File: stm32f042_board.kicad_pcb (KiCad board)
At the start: 4 copper layers, 37.8 x 18.8 mm, 24 parts, among them J1 Conn_01x12_Female, J2 Conn_01x12_Female, J3 USB_B_Micro, J5 JTAG/SWD, U1 STM32F042F6Px, U2 MCP1802, U3 USBLC6-2SC6

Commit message: Bug fixes
- Un-migrate to v7 - oshpark not compatibile yet
- Optionally ground USB shield to board via R 0k
- Route Tx/Rx (USB D+/-) as diff pair to breakout pins
- Fix missing +3V3 connection to JTAG pin 1
- Four-layer board
- Remove unnecessary gaps in copper now that board is four layers
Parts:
- added R1: 0k, Resistor_SMD:R_0603_1608Metric, F.Cu at (176.7, 58.6)
- moved G*** 2.10 mm to (175.7, 72.3), turned to -90 degrees
- moved C4 0.55 mm to (161.5, 67.3)
- moved C3 0.19 mm to (164.4, 66.6)
- moved C5 0.19 mm to (164.4, 64.6)
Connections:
- J3 pad 4: Net-(J3-Pad4) -> unconnected-(J3-Pad4)
- J3 pad 6: GND -> Net-(J3-Pad6)
- J5 pad 6: Net-(J5-Pad6) -> unconnected-(J5-Pad6)
- J5 pad 7: Net-(J5-Pad7) -> unconnected-(J5-Pad7)
- J5 pad 8: Net-(J5-Pad8) -> unconnected-(J5-Pad8)
- U2 pad 4: Net-(U2-Pad4) -> unconnected-(U2-Pad4)
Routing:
- net Net-(J3-Pad6): track 0.00 -> 13.8 mm
- net VBUS: track 49.2 -> 52.2 mm, vias 5 -> 7
- net GND: track 41.6 -> 39.5 mm, vias 10 -> 15
- net USB+: track 24.7 -> 23.3 mm
- net +3V3: track 27.7 -> 27.0 mm, vias 3 -> 5
- net USB-: track 22.0 -> 22.7 mm
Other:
- outline, holes or cut-outs redrawn
- board text added: "STM32F042 breakout, v3 Jed Parsons github.com/jedp/"
- board text added: "VBUS 5V"
- board text removed: "STM32F042 breakout, v2 Jed Parsons github.com/jedp/"

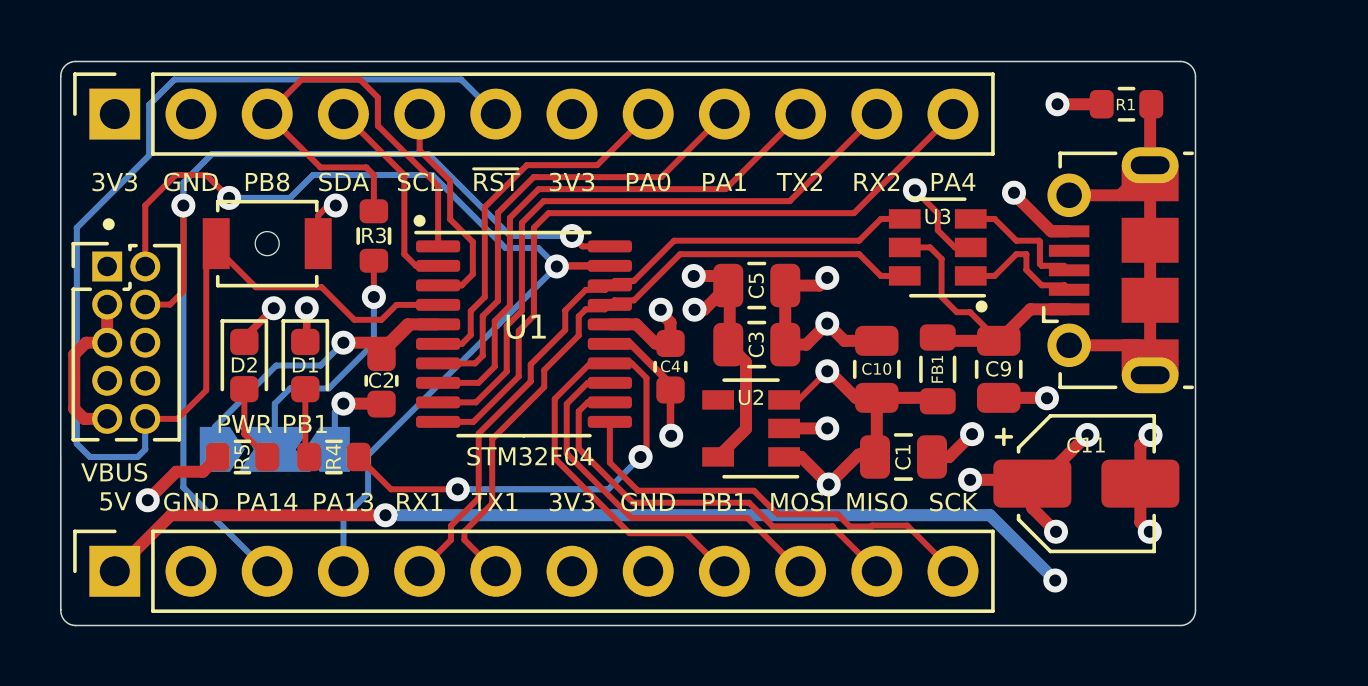
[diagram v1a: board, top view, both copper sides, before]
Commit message: Replace USB Micro receptacle with USB C
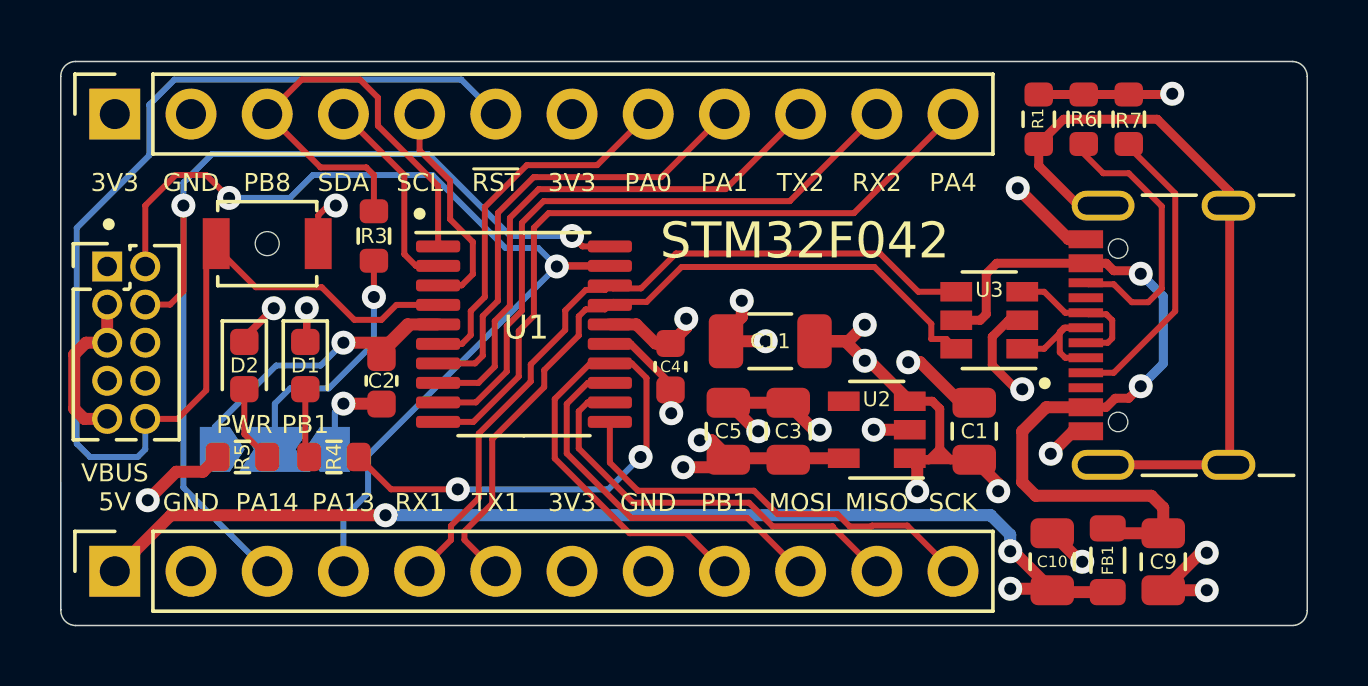
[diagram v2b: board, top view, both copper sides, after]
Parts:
- added R6: 5.1k, Resistor_SMD:R_0603_1608Metric, F.Cu at (175.3, 59.1)
- added R7: 5.1k, Resistor_SMD:R_0603_1608Metric, F.Cu at (176.8, 59.1)
- C11: footprint Capacitor_SMD:CP_Elec_4x4.5 -> Capacitor_SMD:C_1206_3216Metric
- J3: value USB_B_Micro -> USB_C_Receptacle_USB2.0; footprint Connector_USB:USB_Micro-B_Molex-105017-0001 -> Connector_USB:USB_C_Receptacle_GCT_USB4105-xx-A_16P_TopMnt_Horizontal
- moved C11 11.6 mm to (164.8, 66.5), turned to 180 degrees
- moved C10 8.68 mm to (174.2, 73.8)
- moved FB1 8.52 mm to (176.1, 73.8)
- moved C9 8.44 mm to (177.9, 73.8)
- moved G*** 7.56 mm to (179.9, 66.0)
- moved C5 4.95 mm to (163.5, 69.5), turned to 90 degrees
- moved U2 4.19 mm to (168.4, 69.5)
- moved J3 3.52 mm to (179.1, 66.3)
- moved C3 3.07 mm to (165.4, 69.5), turned to 90 degrees
- moved U3 2.97 mm to (172.2, 65.8)
- moved R1 2.97 mm to (173.8, 59.1), turned to 90 degrees
- moved C1 2.51 mm to (171.7, 69.5), turned to 90 degrees
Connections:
- R1 pad 1: Net-(J3-Pad6) -> Net-(J3-PadS1)
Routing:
- net Net-(J3-PadS1): track 0.00 -> 24.5 mm
- net USB_VBUS: track 10.0 -> 26.4 mm, vias 0 -> 2
- net Net-(J3-Pad6): track 13.8 -> 0.00 mm
- net Net-(J3-PadA5): track 0.00 -> 10.0 mm
- net Net-(J3-PadB5): track 0.00 -> 9.37 mm
- net GND: track 39.5 -> 45.7 mm, vias 15 -> 18
- net USB-: track 22.7 -> 25.3 mm
- net +3V3: track 27.0 -> 24.9 mm
- net USB+: track 23.3 -> 25.2 mm
- net USB_D-: track 4.38 -> 5.09 mm
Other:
- board size 37.8 x 18.8 mm -> 41.6 x 18.8 mm
- board text added: "BOOT"
- board text added: "STM32F042"
- board text added: "STM32F042 breakout, v4 Jed Parsons github.com/jedp/"
- board text removed: "STM32F04"
- board text removed: "STM32F042 breakout, v3 Jed Parsons github.com/jedp/"
